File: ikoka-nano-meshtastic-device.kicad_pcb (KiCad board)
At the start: 2 copper layers, 40 x 40 mm, 21 parts, among them J1 Qwiic_RA, J2 Solar, J3 Battery, J4 Battery, Q1 FDN302P, U1 Seeed Studio XIAO nRF52840, U2 E22-900M30S, U3 MT3608

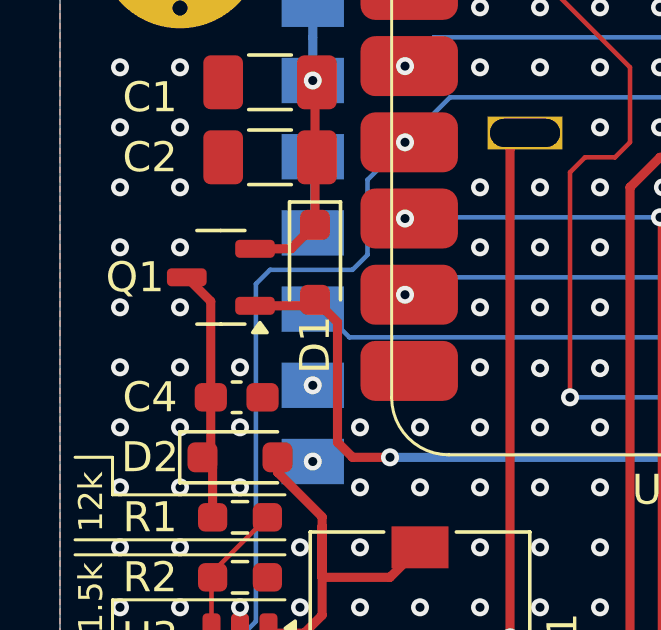
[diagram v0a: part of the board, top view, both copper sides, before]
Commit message: Use AO3401A PMOS which is JLCPCB basic part
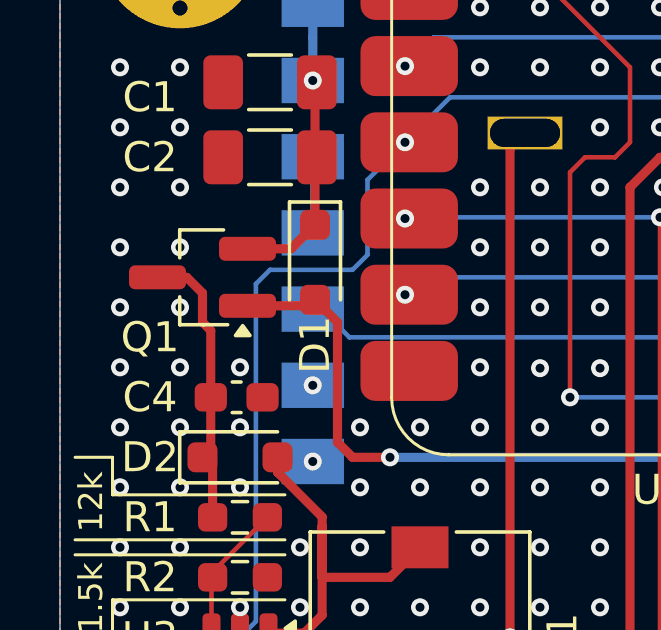
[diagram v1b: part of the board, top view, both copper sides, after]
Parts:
- Q1: value FDN302P -> Q_PMOS_GSD; footprint Package_TO_SOT_SMD:SOT-23-3 -> Package_TO_SOT_SMD:SOT-23_Handsoldering
- moved Q1 0.61 mm to (134.8, 95.0)
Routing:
- net 5V: track 8.59 -> 9.56 mm
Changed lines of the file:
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@@
 			)
 		)
-		(property "LCSC" "C153761"
+		(property "LCSC" "C191023"
 			(at 0 0 0)
 			(unlocked yes)
@@
 		)
 	)
-	(footprint "Package_TO_SOT_SMD:SOT-23-3"
+	(footprint "Package_TO_SOT_SMD:SOT-23_Handsoldering"
 		(layer "F.Cu")
-		(at 135.3625 95 180)
-		(descr "SOT, 3 Pin (JEDEC MO-178 inferred 3-pin variant https://www.jedec.org/document_search?search_api_views_fulltext=MO-178), generated with kicad-footprint-generator ipc_gullwing_generator.py")
-		(tags "SOT TO_SOT_SMD")
+		(at 134.75 95 180)
+		(descr "SOT-23, Handsoldering")
+		(tags "SOT-23")
 		(property "Reference" "Q1"
-			(at 2.8625 0 0)
+			(at 1.75 -2 180)
 			(layer "F.SilkS")
 			(effects
@@
 			)
 		)
-		(property "Value" "FDN302P"
-			(at 0 2.4 0)
+		(property "Value" "Q_PMOS_GSD"
+			(at 0 2.5 180)
 			(layer "F.Fab")
-			(hide yes)
 			(effects
 				(font
@@
 			)
 		)
-		(property "Footprint" "Package_TO_SOT_SMD:SOT-23-3"
-			(at 0 0 0)
+		(property "Footprint" "Package_TO_SOT_SMD:SOT-23_Handsoldering"
+			(at 0 0 180)
+			(unlocked yes)
 			(layer "F.Fab")
 			(hide yes)
@@
 			)
 		)
-		(property "Datasheet" "https://www.lcsc.com/datasheet/lcsc_datasheet_2410010102_onsemi-FDN302P_C3280162.pdf"
-			(at 0 0 0)
+		(property "Datasheet" ""
+			(at 0 0 180)
+			(unlocked yes)
 			(layer "F.Fab")
 			(hide yes)
@@
 			)
 		)
-		(property "Description" "20V 2.4A 55mΩ@2.4A,4.5V 500mW 1.5V@250uA 1 Piece P-Channel SOT-23-3 MOSFETs ROHS"
-			(at 0 0 0)
+		(property "Description" "P-MOSFET transistor, gate/source/drain"
+			(at 0 0 180)
+			(unlocked yes)
 			(layer "F.Fab")
 			(hide yes)
@@
 			)
 		)
-		(property "LCSC" "C3280162"
+		(property "LCSC" "C15127"
 			(at 0 0 180)
 			(unlocked yes)
@@
 		(attr smd)
 		(fp_line
-			(start 0 1.56)
-			(end 0.8 1.56)
+			(start 0.76 1.58)
+			(end 0.76 0.65)
 			(stroke
 				(width 0.12)
@@
 		)
 		(fp_line
-			(start 0 1.56)
-			(end -0.8 1.56)
+			(start 0.76 1.58)
+			(end -0.7 1.58)
 			(stroke
 				(width 0.12)
@@
 		)
 		(fp_line
-			(start 0 -1.56)
-			(end 0.8 -1.56)
+			(start 0.76 -1.58)
+			(end 0.76 -0.65)
 			(stroke
 				(width 0.12)
@@
 		)
 		(fp_line
-			(start 0 -1.56)
-			(end -0.8 -1.56)
+			(start -0.04 -1.58)
+			(end 0.76 -1.58)
+			(stroke
+				(width 0.12)
+				(type solid)
+			)
+			(layer "F.SilkS")
+		)
+		(fp_line
+			(start -0.04 -1.58)
+			(end -0.84 -1.58)
 			(stroke
 				(width 0.12)
@@
 		(fp_poly
 			(pts
-				(xy -1.3 -1.51) (xy -1.54 -1.84) (xy -1.06 -1.84) (xy -1.3 -1.51)
+				(xy -1.34 -1.61) (xy -1.58 -1.94) (xy -1.1 -1.94) (xy -1.34 -1.61)
 			)
 			(stroke
@@
 		)
 		(fp_line
-			(start 2.05 1.7)
-			(end 2.05 -1.7)
+			(start 2.7 1.75)
+			(end -2.7 1.75)
 			(stroke
 				(width 0.05)
@@
 		)
 		(fp_line
-			(start 2.05 -1.7)
-			(end -2.05 -1.7)
+			(start 2.7 -1.75)
+			(end 2.7 1.75)
 			(stroke
 				(width 0.05)
@@
 		)
 		(fp_line
-			(start -2.05 1.7)
-			(end 2.05 1.7)
+			(start -2.7 1.75)
+			(end -2.7 -1.75)
 			(stroke
 				(width 0.05)
@@
 		)
 		(fp_line
-			(start -2.05 -1.7)
-			(end -2.05 1.7)
+			(start -2.7 -1.75)
+			(end 2.7 -1.75)
 			(stroke
 				(width 0.05)
@@
 		)
 		(fp_line
-			(start 0.8 1.45)
-			(end -0.8 1.45)
+			(start 0.7 -1.52)
+			(end 0.7 1.52)
 			(stroke
 				(width 0.1)
@@
 		)
 		(fp_line
-			(start 0.8 -1.45)
-			(end 0.8 1.45)
+			(start -0.15 -1.52)
+			(end 0.7 -1.52)
 			(stroke
 				(width 0.1)
@@
 		)
 		(fp_line
-			(start -0.4 -1.45)
-			(end 0.8 -1.45)
+			(start -0.7 1.52)
+			(end 0.7 1.52)
 			(stroke
 				(width 0.1)
@@
 		)
 		(fp_line
-			(start -0.8 1.45)
-			(end -0.8 -1.05)
+			(start -0.7 -0.95)
+			(end -0.15 -1.52)
 			(stroke
 				(width 0.1)
@@
 		)
 		(fp_line
-			(start -0.8 -1.05)
-			(end -0.4 -1.45)
+			(start -0.7 -0.95)
+			(end -0.7 1.5)
 			(stroke
 				(width 0.1)
@@
 		)
 		(fp_text user "${REFERENCE}"
-			(at 0 0 0)
+			(at 0 0 -90)
 			(layer "F.Fab")
 			(effects
 				(font
-					(size 0.4 0.4)
-					(thickness 0.06)
+					(size 0.5 0.5)
+					(thickness 0.075)
 				)
 			)
 		)
 		(pad "1" smd roundrect
-			(at -1.1375 -0.95 180)
-			(size 1.325 0.6)
+			(at -1.5 -0.95 180)
+			(size 1.9 0.8)
 			(layers "F.Cu" "F.Paste" "F.Mask")
 			(roundrect_rratio 0.25)
@@
 		)
 		(pad "2" smd roundrect
-			(at -1.1375 0.95 180)
-			(size 1.325 0.6)
+			(at -1.5 0.95 180)
+			(size 1.9 0.8)
 			(layers "F.Cu" "F.Paste" "F.Mask")
 			(roundrect_rratio 0.25)
@@
 		)
 		(pad "3" smd roundrect
-			(at 1.1375 0 180)
-			(size 1.325 0.6)
+			(at 1.5 0 180)
+			(size 1.9 0.8)
 			(layers "F.Cu" "F.Paste" "F.Mask")
 			(roundrect_rratio 0.25)
@@
 			(pintype "passive")
 		)
-		(model "${KICAD8_3DMODEL_DIR}/Package_TO_SOT_SMD.3dshapes/SOT-23-3.wrl"
+		(model "${KICAD8_3DMODEL_DIR}/Package_TO_SOT_SMD.3dshapes/SOT-23.wrl"
 			(offset
 				(xyz 0 0 0)
@@
 			(thermal_bridge_angle 0)
 		)
-		(model "${SPARKFUN_KICAD_LIBRARY}/Footprints/SparkFun-3D-models/Connector/Qwiic-Horizontal.STEP"
-			(offset
-				(xyz 0 -0.5 -0.3)
-			)
-			(scale
-				(xyz 1 1 1)
-			)
-			(rotate
-				(xyz -90 0 0)
-			)
-		)
 		(model "${KIPRJMOD}/symbols/SparkFun-KiCad-Libraries/Footprints/SparkFun-3D-models/Connector/Qwiic-Horizontal-White.STEP"
 			(offset
@@
 	)
 	(segment
-		(start 139.25 100.5)
-		(end 139.75 101)
+		(start 139.25 96.5)
+		(end 139.25 100.5)
+		(width 0.3048)
+		(layer "F.Cu")
+		(net 23)
+	)
+	(segment
+		(start 136.25 95.95)
+		(end 138.7 95.95)
 		(width 0.3048)
 		(layer "F.Cu")
@@
 	)
 	(segment
-		(start 139.75 101)
-		(end 141 101)
+		(start 139.25 100.5)
+		(end 139.75 101)
 		(width 0.3048)
 		(layer "F.Cu")
@@
 	)
 	(segment
-		(start 136.5 95.95)
-		(end 138.7 95.95)
+		(start 139.75 101)
+		(end 141 101)
 		(width 0.3048)
 		(layer "F.Cu")
@@
 	)
 	(segment
-		(start 139.25 96.5)
-		(end 139.25 100.5)
-		(width 0.3048)
-		(layer "F.Cu")
-		(net 23)
-	)
-	(segment
 		(start 161 84.5)
 		(end 159.38 82.88)
@@
 	)
 	(segment
-		(start 136.5 94.05)
-		(end 137.7 94.05)
+		(start 137.7 94.05)
+		(end 138.5 93.25)
 		(width 0.3048)
 		(layer "F.Cu")
@@
 	)
 	(segment
-		(start 137.7 94.05)
-		(end 138.5 93.25)
+		(start 136.25 94.05)
+		(end 137.7 94.05)
 		(width 0.3048)
 		(layer "F.Cu")
@@
 	)
 	(segment
-		(start 135.025 99)
-		(end 135.025 95.8)
+		(start 135.025 96.775)
+		(end 134.75 96.5)
+		(width 0.3048)
+		(layer "F.Cu")
+		(net 29)
+	)
+	(segment
+		(start 134.225 95)
+		(end 133.25 95)
 		(width 0.3048)
 		(layer "F.Cu")
@@
 	)
 	(segment
-		(start 135.025 95.8)
-		(end 134.225 95)
+		(start 135.025 99)
+		(end 135.025 100.725)
 		(width 0.3048)
 		(layer "F.Cu")
@@
 	(segment
 		(start 135.025 99)
-		(end 135.025 100.725)
+		(end 135.025 96.775)
 		(width 0.3048)
 		(layer "F.Cu")
@@
 		(width 0.3048)
 		(layer "F.Cu")
+		(net 29)
+	)
+	(segment
+		(start 134.75 95.525)
+		(end 134.225 95)
+		(width 0.3048)
+		(layer "F.Cu")
+		(net 29)
+	)
+	(segment
+		(start 134.75 96.5)
+		(end 134.75 95.525)
+		(width 0.3048)
+		(layer "F.Cu")
